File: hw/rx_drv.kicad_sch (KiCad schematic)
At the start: 7 parts, among them U35 SN75176AD

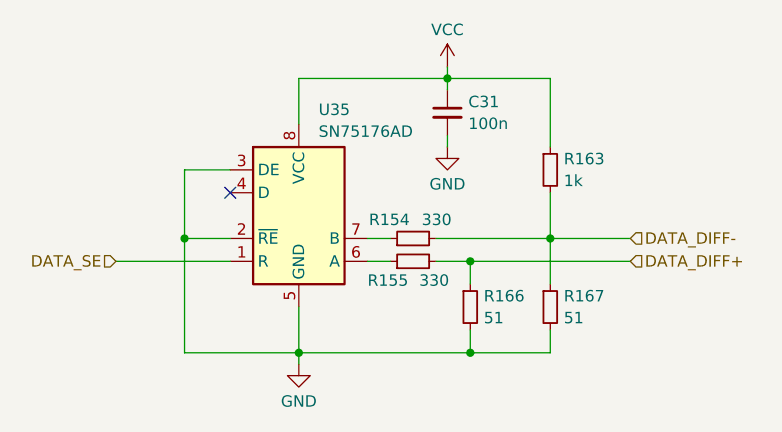
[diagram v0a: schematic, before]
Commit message: BUS*B* Parity bit driver direction pin was accidentally connected to BUS*A* direction net
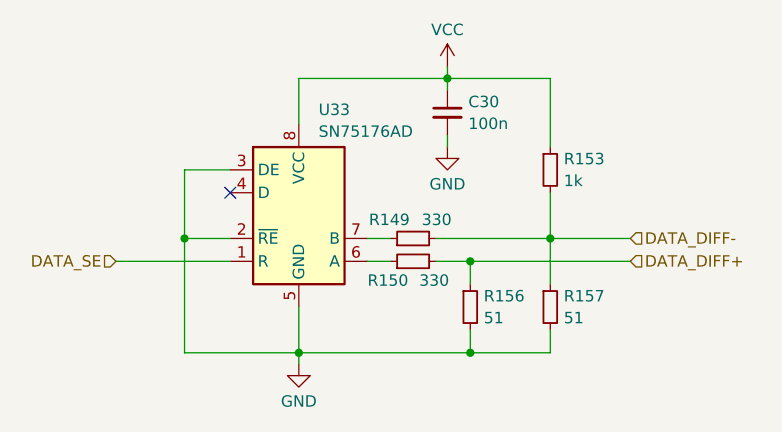
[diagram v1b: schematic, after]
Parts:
- renumbered C31 to C30, R154 to R149, R155 to R150, R163 to R153, R166 to R156, R167 to R157, U35 to U33
